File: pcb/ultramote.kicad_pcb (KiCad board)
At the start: 2 copper layers, 40 x 42.5 mm, 59 parts, among them J1 U.FL-R-SMT-1, J2 SM02B-SRSS-TB, J3 918-418K2023S40001, J5 Conn_01x04, J6 PJ-242D-SMT, J7 PJ-242D-SMT, Q1 2N7002, Q2 BSS84, SW1 SSSS211603, U1 LoRa-E5, U2 TPS2112APW, U3 MCP73831-5-OT, U4 TLV70233DBVT, U5 CH340N, U6 EL357, U7 EL357

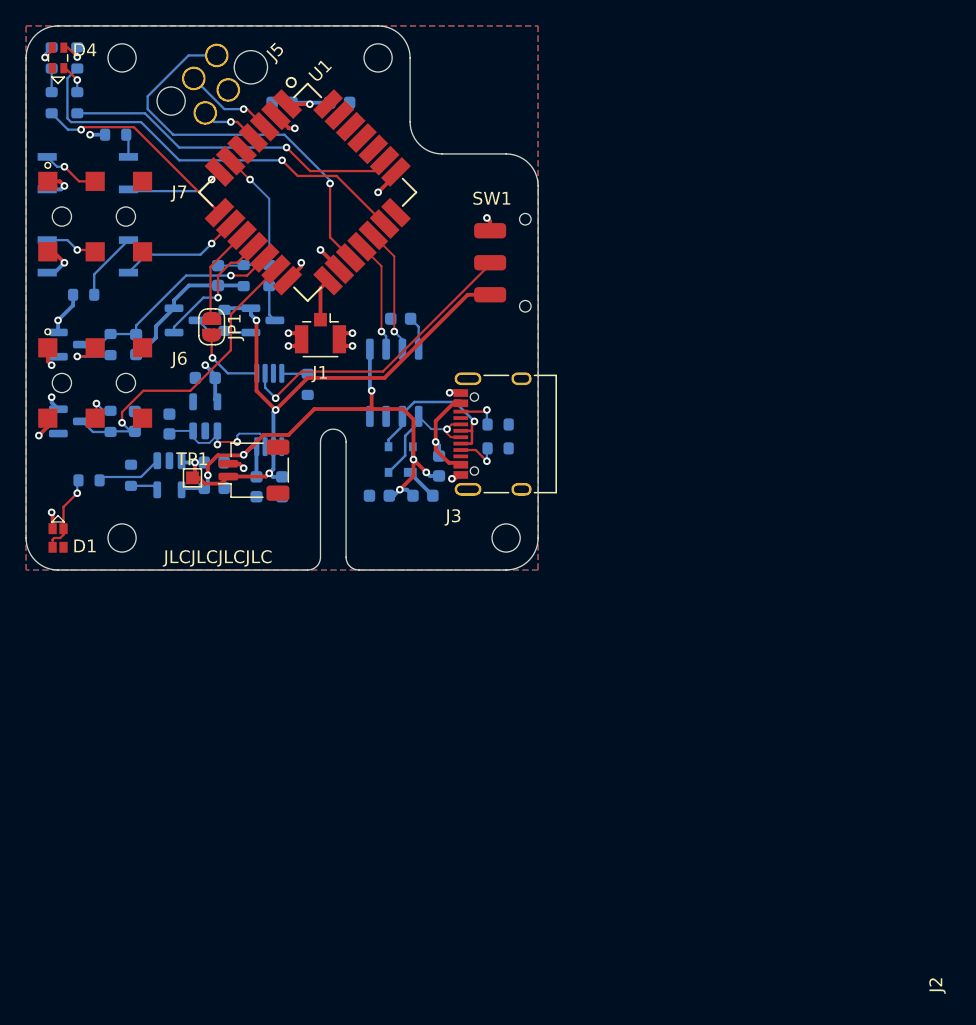
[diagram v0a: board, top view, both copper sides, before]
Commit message: Add Mounting Holes as schematic symbol
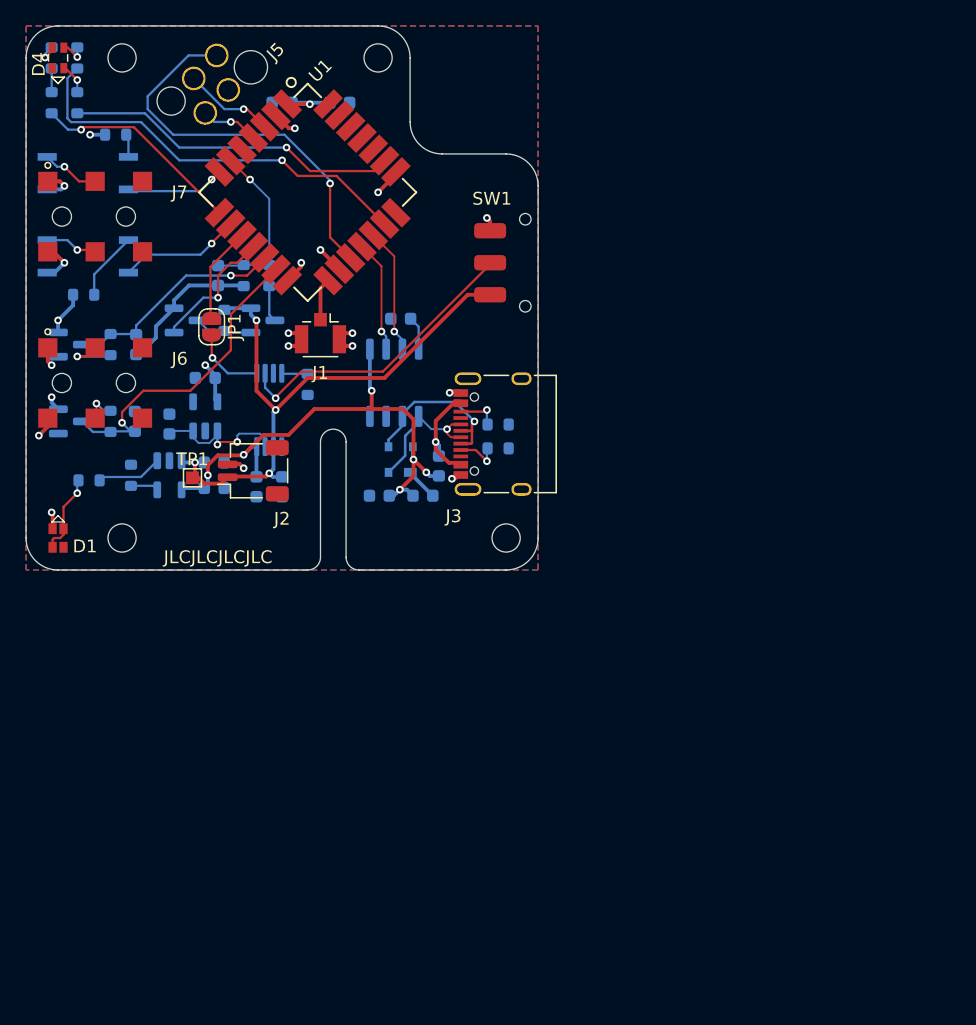
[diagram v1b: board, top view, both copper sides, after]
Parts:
- removed REF** (x4): MountingHole_2.2mm_M2, MountingHole:MountingHole_2.2mm_M2
- added H1: MountingHole, MountingHole:MountingHole_2.2mm_M2, F.Cu at (100.5, 59.6)
- added H2: MountingHole, MountingHole:MountingHole_2.2mm_M2, F.Cu at (120.5, 59.6)
- added H3: MountingHole, MountingHole:MountingHole_2.2mm_M2, F.Cu at (100.5, 97.1)
- added H4: MountingHole, MountingHole:MountingHole_2.2mm_M2, F.Cu at (130.5, 97.1)
- J3: value 918-418K2023S40001 -> USB-C-XKB_U262-16XN
- J5: value Conn_01x04 -> WST-REDFIT-4P
- moved J2 0.07 mm to (110.8, 91.9)
- turned FB1 to -90 degrees
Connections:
- FB1 pad 1: VBUS -> Net-(FB1-Pad1)
- FB1 pad 2: Net-(FB1-Pad2) -> VBUS
- J3 pad A4: Net-(FB1-Pad2) -> Net-(FB1-Pad1)
- J3 pad A9: Net-(FB1-Pad2) -> Net-(FB1-Pad1)
- J3 pad B4: Net-(FB1-Pad2) -> Net-(FB1-Pad1)
- J3 pad B9: Net-(FB1-Pad2) -> Net-(FB1-Pad1)
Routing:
- net Net-(FB1-Pad2): track 8.42 -> 0.00 mm, vias 1 -> 0
- net Net-(FB1-Pad1): track 0.00 -> 8.42 mm, vias 0 -> 1
